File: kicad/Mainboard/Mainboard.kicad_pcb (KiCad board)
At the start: 2 copper layers, 46.9 x 107.1 mm, 277 parts, among them J1 ESP8266 module, J10 MIC_EXT, J11 VIB2, J12 SPK_EXT, J13 GPS_CONN, J14 Micro_SD_Card, J15 DBG_CONN, J3 USB_OTG, J4 SWD, J5 BATT, J6 POT_PWR_SW, J7 Conn_01x10, J8 Antenna, J9 VIB1, Q1 BSS138, Q2 BSS138, Q3 BGA6589, Q4 BSS138, Q5 BSS138, Q6 BSS138, Q7 FDV304P, SW1 INT_PTT_SW, T1 AFT05MS004NT1, U1 STM32F777VIT, U10 LM386, U11 LSM9DS1, U13 BGA2874, U2 USBLC6-2SC6, U3 LD1117S50TR_SOT223, U4 LD1117S33TR_SOT223, U5 ADF7021, U6 HMC546MS8GETR, U7 LM2904A, U8 HEF4066B, U9 OPA340UA, X1 12.288MHz

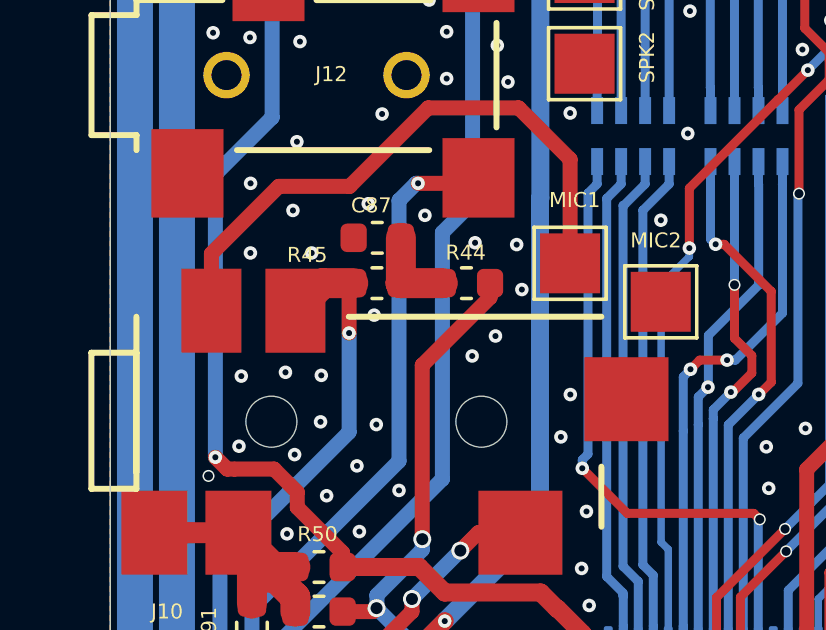
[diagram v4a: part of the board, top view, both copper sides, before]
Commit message: added Jumper cable connections description -> moved "M17" and "TR-9" labels -> added label "v 2.0" -> plotted PDF
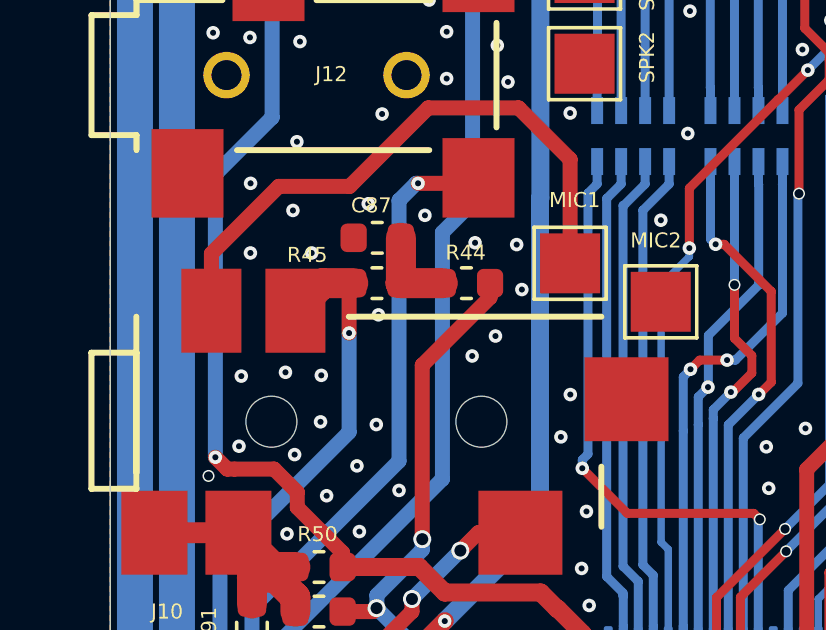
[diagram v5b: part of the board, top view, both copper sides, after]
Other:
- board text added: "v2.0"
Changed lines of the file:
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@@
   (general
     (thickness 1.6)
-    (drawings 66)
+    (drawings 67)
     (tracks 3351)
     (zones 0)
@@
   )
   (setup
-    (last_trace_width 1)
+    (last_trace_width 0.25)
     (user_trace_width 0.2)
     (user_trace_width 0.25)
@@
     )
   )
+  (gr_text "v2.0\n" (at 21.44268 130.98272) (layer B.SilkS)
+    (effects (font (size 1.3 1.3) (thickness 0.25)) (justify mirror))
+  )
   (gr_text "write\nsomething:" (at 46.355 72.263) (layer B.SilkS)
     (effects (font (size 0.7 0.7) (thickness 0.15)) (justify mirror))
@@
     (effects (font (size 1.5 1.5) (thickness 0.3)))
   )
-  (gr_text TR-9 (at 24.6888 115.2652) (layer B.SilkS)
-    (effects (font (size 1.8 1.8) (thickness 0.28)) (justify mirror))
+  (gr_text TR-9 (at 24.0284 128.40716) (layer B.SilkS)
+    (effects (font (size 2.2 2.2) (thickness 0.35)) (justify mirror))
   )
-  (gr_text M17 (at 25.1968 113.284) (layer B.SilkS)
-    (effects (font (size 1 1) (thickness 0.15)) (justify mirror))
+  (gr_text M17 (at 28.31592 125.84684) (layer B.SilkS)
+    (effects (font (size 1.3 1.3) (thickness 0.25)) (justify mirror))
   )
   (gr_text "Schematic by:\nWojtek SP5WWP,\nMathis DB9MAT et al." (at 36.1188 118.364) (layer B.SilkS)
@@
   (via (at 32.77108 127.21336) (size 0.45) (drill 0.2) (layers F.Cu B.Cu) (net 1))
   (via (at 31.89224 128.76276) (size 0.45) (drill 0.2) (layers F.Cu B.Cu) (net 1))
-  (via (at 27.84856 128.0668) (size 0.45) (drill 0.2) (layers F.Cu B.Cu) (net 1))
+  (via (at 27.9908 128.05664) (size 0.45) (drill 0.2) (layers F.Cu B.Cu) (net 1))
   (via (at 23.7236 125.99416) (size 0.45) (drill 0.2) (layers F.Cu B.Cu) (net 1))
   (via (at 25.14092 124.57684) (size 0.45) (drill 0.2) (layers F.Cu B.Cu) (net 1))

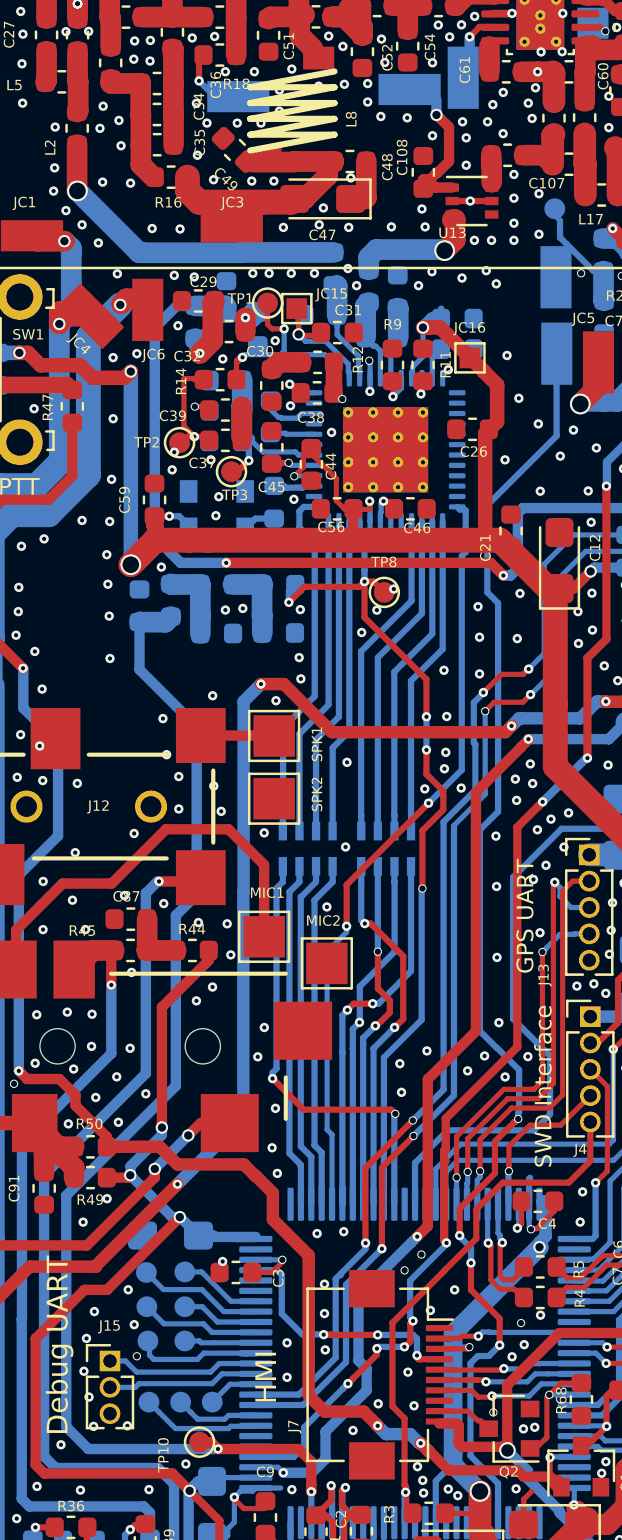
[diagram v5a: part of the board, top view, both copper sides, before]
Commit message: changed OscillatorON to XO_EN -> added "SN:" title on PCB -> plotted new PDF
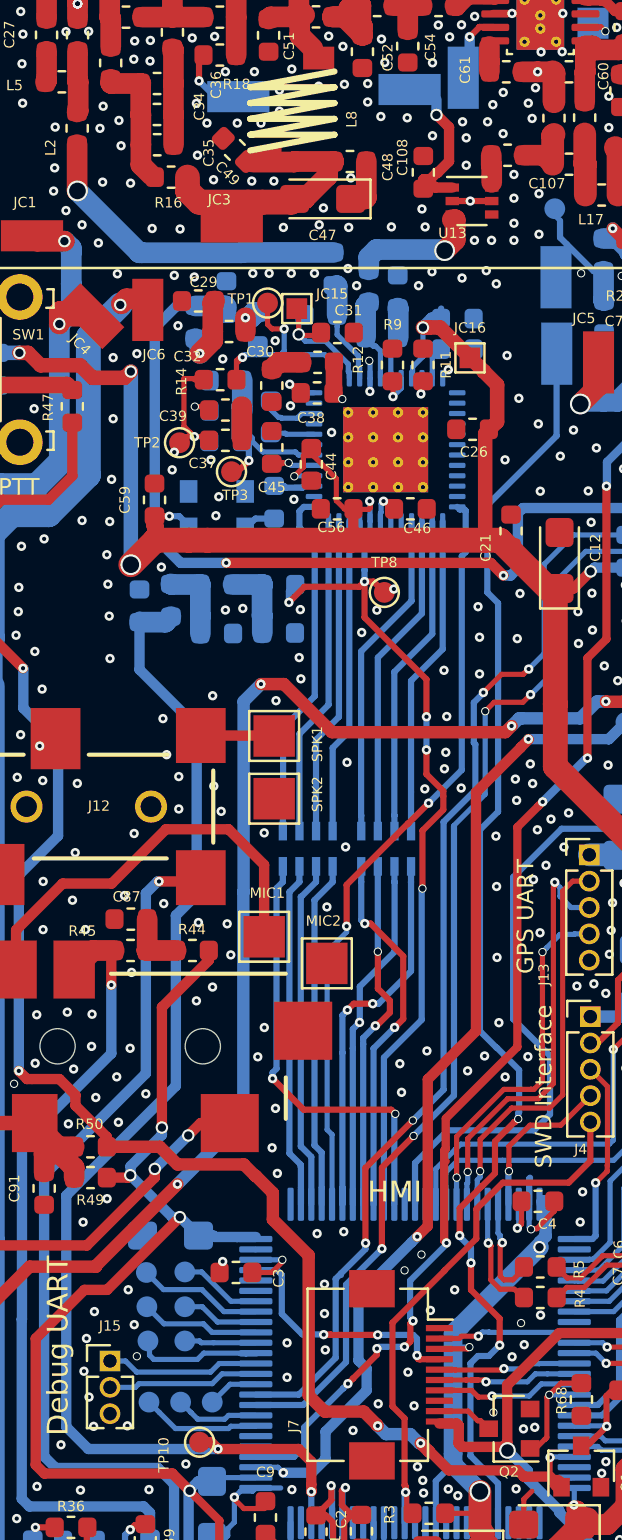
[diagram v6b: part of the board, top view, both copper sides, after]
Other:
- board text added: "SN:"
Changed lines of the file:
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@@
   (general
     (thickness 1.6)
-    (drawings 67)
+    (drawings 68)
     (tracks 3351)
     (zones 0)
@@
   (module TR-9:Pad1x3 (layer B.Cu)
     (at 46.7995 98.2853 270)
-    (fp_text reference JC14 (at 2.5527 -1.778 270) (layer B.SilkS)
+    (fp_text reference JC14 (at 2.9591 -1.67386 270) (layer B.SilkS)
       (effects (font (size 0.5 0.5) (thickness 0.15)) (justify mirror))
     )
@@
   (module TR-9:Pad1x3 (layer B.Cu)
     (at 50.1269 94.5007 90)
-    (fp_text reference JC12 (at 1.9939 -1.1557 180) (layer B.SilkS)
+    (fp_text reference JC12 (at 2.10058 -0.8763 180) (layer B.SilkS)
       (effects (font (size 0.5 0.5) (thickness 0.15)) (justify mirror))
     )
@@
   (module TR-9:Pad1x3 (layer B.Cu)
     (at 62.3062 78.2574)
-    (fp_text reference JC10 (at 0 -0.5) (layer B.SilkS)
+    (fp_text reference JC10 (at -0.01524 -0.12192) (layer B.SilkS)
       (effects (font (size 0.5 0.5) (thickness 0.15)) (justify mirror))
     )
@@
   (module TR-9:Pad1x3 (layer F.Cu)
     (at 32.8676 90.4494)
-    (fp_text reference JC3 (at 0 0.5) (layer F.SilkS)
+    (fp_text reference JC3 (at -0.65024 0.36068) (layer F.SilkS)
       (effects (font (size 0.5 0.5) (thickness 0.15)))
     )
@@
     (tags capacitor)
     (attr smd)
-    (fp_text reference C49 (at 0.70114 1.31572 135) (layer F.SilkS)
+    (fp_text reference C49 (at 0.545169 1.052486 135) (layer F.SilkS)
       (effects (font (size 0.5 0.5) (thickness 0.15)))
     )
@@
     (tags capacitor)
     (attr smd)
-    (fp_text reference C35 (at 2.06766 -0.1016 90) (layer F.SilkS)
+    (fp_text reference C35 (at 2.48422 0.38862 90) (layer F.SilkS)
       (effects (font (size 0.5 0.5) (thickness 0.15)))
     )
@@
     )
   )
+  (gr_text SN: (at 43.85564 123.31192) (layer B.SilkS)
+    (effects (font (size 1 1) (thickness 0.15)) (justify mirror))
+  )
   (gr_text "v2.0\n" (at 21.44268 130.98272) (layer B.SilkS)
     (effects (font (size 1.3 1.3) (thickness 0.25)) (justify mirror))
@@
     (effects (font (size 1 1) (thickness 0.15)))
   )
-  (gr_text HMI (at 34.48812 147.56384 90) (layer F.SilkS)
+  (gr_text HMI (at 40.67048 138.6332) (layer F.SilkS)
     (effects (font (size 1 1) (thickness 0.15)))
   )

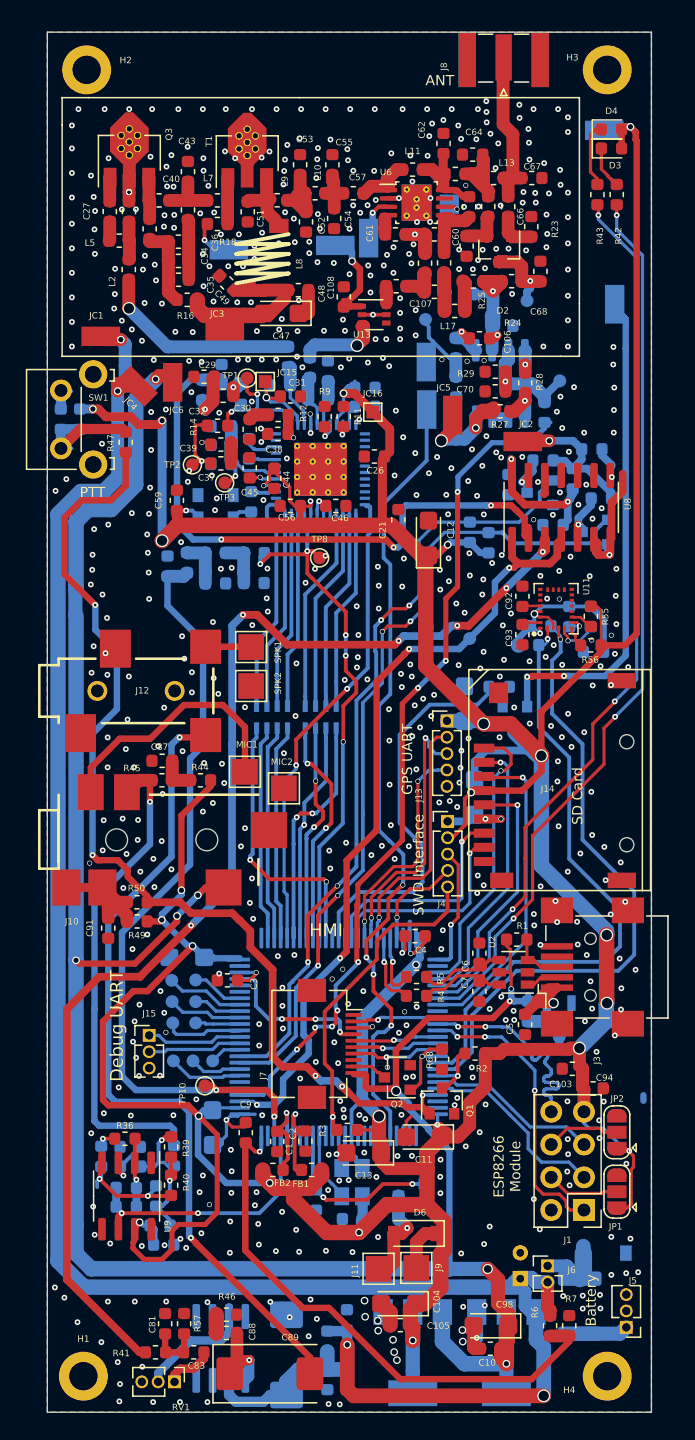
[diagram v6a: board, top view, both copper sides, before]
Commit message: optimized vias sizes
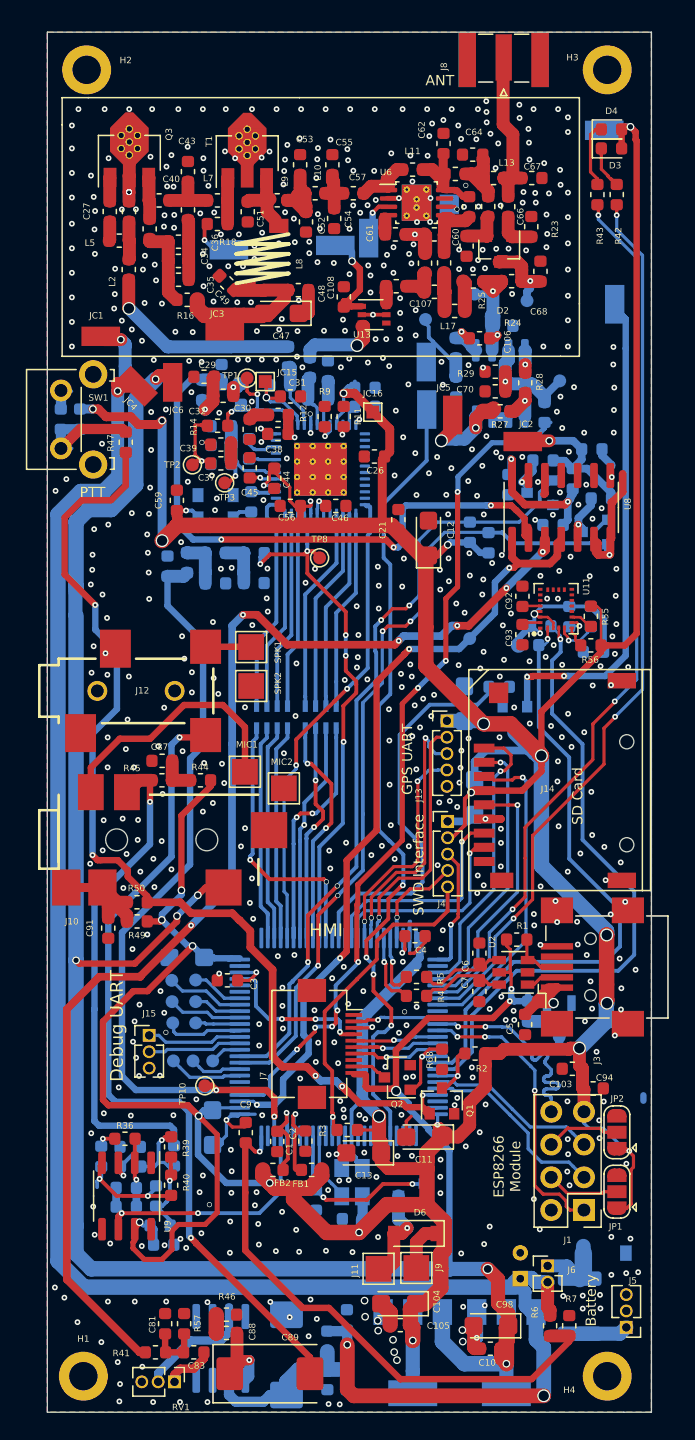
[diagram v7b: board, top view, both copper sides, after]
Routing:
- net +3V3: track 445.9 -> 446.6 mm, vias 32 -> 31
- net Net-(C38-Pad2): track 3.43 -> 4.16 mm
- net ADF_SWD: vias 6 -> 5
- net GND: vias 638 -> 643
